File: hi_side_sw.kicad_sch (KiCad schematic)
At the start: 10 parts, among them Q16 MMBT2222A, Q17 WST03P06, Q18 S9015, Q19 MMBT2222A

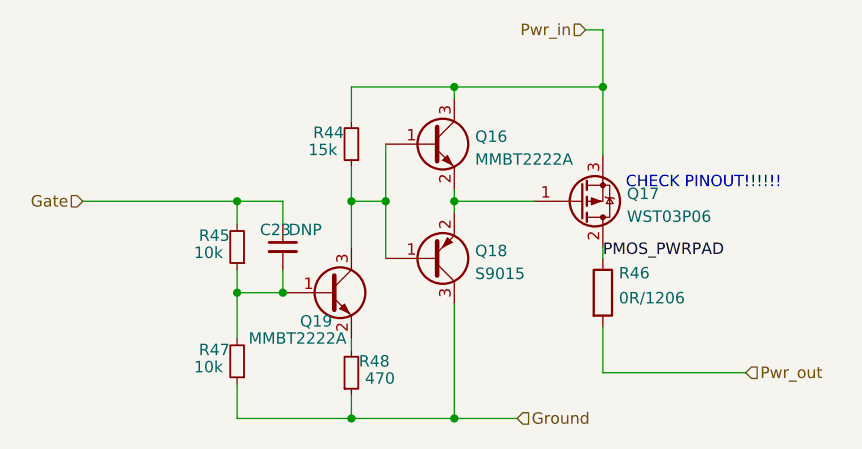
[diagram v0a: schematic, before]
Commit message: replace audio with IOexp + PD controller, project rename
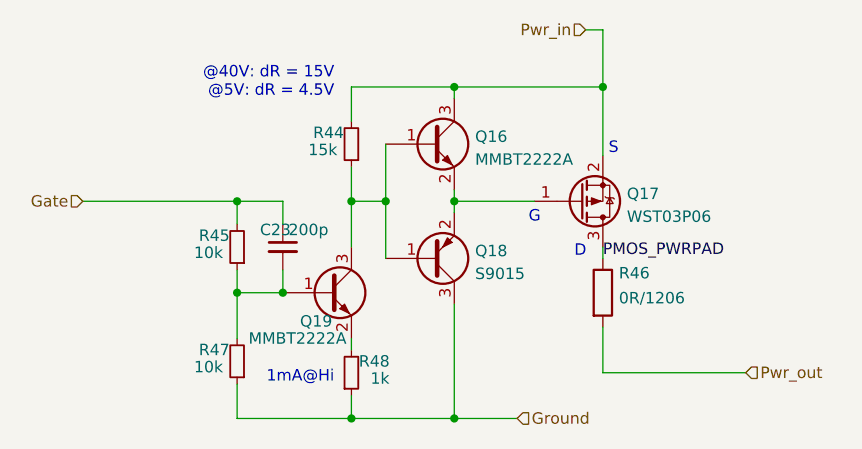
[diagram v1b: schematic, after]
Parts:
- C23: value DNP -> 200p; LCSC (none) -> C1530
- Q16, Q19: LCSC (none) -> C8512
- R44, R45, R47: LCSC C25117 -> (none)
- R48: value 470 -> 1k; LCSC C25117 -> (none)
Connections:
- net PMOS_PWRPAD: now also Q17.3 (S); no longer Q17.2 (S)
- net Pwr_in: now also Q17.2 (D); no longer Q17.3 (D)
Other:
- note added: "1mA@Hi"
- note added: "@40V: dR = 15V @5V: dR = 4.5V"
- note added: "D"
- note added: "G"
- note added: "S"
- note removed: "CHECK PINOUT!!!!!!"

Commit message: production
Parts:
- Q17: LCSC (none) -> C105166
- Q18: LCSC (none) -> C2149
- R44: LCSC (none) -> C25756
- R45, R47: LCSC (none) -> C25744
- R46: LCSC (none) -> C17888
- R48: LCSC (none) -> C11702
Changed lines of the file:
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@@
       (effects (font (size 1.27 1.27)) hide)
     )
-    (property "LCSC" "" (at 108.585 73.66 0)
-      (effects (font (size 1.27 1.27)) hide)
-    )
-    (pin "1")
-    (pin "2")
-    (instances
-      (project "cringenode"
+    (property "LCSC" "C25756" (at 108.585 73.66 0)
+      (effects (font (size 1.27 1.27)) hide)
+    )
+    (pin "1")
+    (pin "2")
+    (instances
+      (project "MOSNode"
         (path "/030e8303-6e45-42d5-8b9a-859414965308/e4a0c18b-f3f3-4251-8bd0-728351d793cd"
           (reference "R44") (unit 1)
@@
       (effects (font (size 1.27 1.27)) (justify left) hide)
     )
+    (property "LCSC" "C105166" (at 133.985 80.01 0)
+      (effects (font (size 1.27 1.27)) hide)
+    )
     (pin "1")
     (pin "2")
     (pin "3")
     (instances
-      (project "cringenode"
+      (project "MOSNode"
         (path "/030e8303-6e45-42d5-8b9a-859414965308/e4a0c18b-f3f3-4251-8bd0-728351d793cd"
           (reference "Q17") (unit 1)
@@
       (effects (font (size 1.27 1.27)) hide)
     )
-    (property "LCSC" "" (at 95.885 85.09 0)
-      (effects (font (size 1.27 1.27)) hide)
-    )
-    (pin "1")
-    (pin "2")
-    (instances
-      (project "cringenode"
+    (property "LCSC" "C25744" (at 95.885 85.09 0)
+      (effects (font (size 1.27 1.27)) hide)
+    )
+    (pin "1")
+    (pin "2")
+    (instances
+      (project "MOSNode"
         (path "/030e8303-6e45-42d5-8b9a-859414965308/e4a0c18b-f3f3-4251-8bd0-728351d793cd"
           (reference "R45") (unit 1)
@@
       (effects (font (size 1.27 1.27)) hide)
     )
+    (property "LCSC" "C2149" (at 117.475 86.36 0)
+      (effects (font (size 1.27 1.27)) hide)
+    )
     (pin "1")
     (pin "2")
     (pin "3")
     (instances
-      (project "cringenode"
+      (project "MOSNode"
         (path "/030e8303-6e45-42d5-8b9a-859414965308/e4a0c18b-f3f3-4251-8bd0-728351d793cd"
           (reference "Q18") (unit 1)
@@
       (effects (font (size 1.27 1.27)) hide)
     )
-    (property "LCSC" "" (at 108.585 99.06 0)
-      (effects (font (size 1.27 1.27)) hide)
-    )
-    (pin "1")
-    (pin "2")
-    (instances
-      (project "cringenode"
+    (property "LCSC" "C11702" (at 108.585 99.06 0)
+      (effects (font (size 1.27 1.27)) hide)
+    )
+    (pin "1")
+    (pin "2")
+    (instances
+      (project "MOSNode"
         (path "/030e8303-6e45-42d5-8b9a-859414965308/e4a0c18b-f3f3-4251-8bd0-728351d793cd"
           (reference "R48") (unit 1)
@@
       (effects (font (size 1.27 1.27)) hide)
     )
-    (pin "1")
-    (pin "2")
-    (instances
-      (project "cringenode"
+    (property "LCSC" "C17888" (at 136.525 90.17 0)
+      (effects (font (size 1.27 1.27)) hide)
+    )
+    (pin "1")
+    (pin "2")
+    (instances
+      (project "MOSNode"
         (path "/030e8303-6e45-42d5-8b9a-859414965308/e4a0c18b-f3f3-4251-8bd0-728351d793cd"
           (reference "R46") (unit 1)
@@
     (pin "3")
     (instances
-      (project "cringenode"
+      (project "MOSNode"
         (path "/030e8303-6e45-42d5-8b9a-859414965308/e4a0c18b-f3f3-4251-8bd0-728351d793cd"
           (reference "Q19") (unit 1)
@@
       (effects (font (size 1.27 1.27)) hide)
     )
-    (property "LCSC" "" (at 95.885 97.79 0)
-      (effects (font (size 1.27 1.27)) hide)
-    )
-    (pin "1")
-    (pin "2")
-    (instances
-      (project "cringenode"
+    (property "LCSC" "C25744" (at 95.885 97.79 0)
+      (effects (font (size 1.27 1.27)) hide)
+    )
+    (pin "1")
+    (pin "2")
+    (instances
+      (project "MOSNode"
         (path "/030e8303-6e45-42d5-8b9a-859414965308/e4a0c18b-f3f3-4251-8bd0-728351d793cd"
           (reference "R47") (unit 1)
@@
     (pin "2")
     (instances
-      (project "cringenode"
+      (project "MOSNode"
         (path "/030e8303-6e45-42d5-8b9a-859414965308/e4a0c18b-f3f3-4251-8bd0-728351d793cd"
           (reference "C23") (unit 1)
@@
     (pin "3")
     (instances
-      (project "cringenode"
+      (project "MOSNode"
         (path "/030e8303-6e45-42d5-8b9a-859414965308/e4a0c18b-f3f3-4251-8bd0-728351d793cd"
           (reference "Q16") (unit 1)
